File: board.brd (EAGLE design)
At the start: 94.6 x 90.5 mm, 65 parts, among them K1 FTR-K1C, K2 FTR-K1C, K3 FTR-K1C, K4 FTR-K1C, X6 PN61729-S

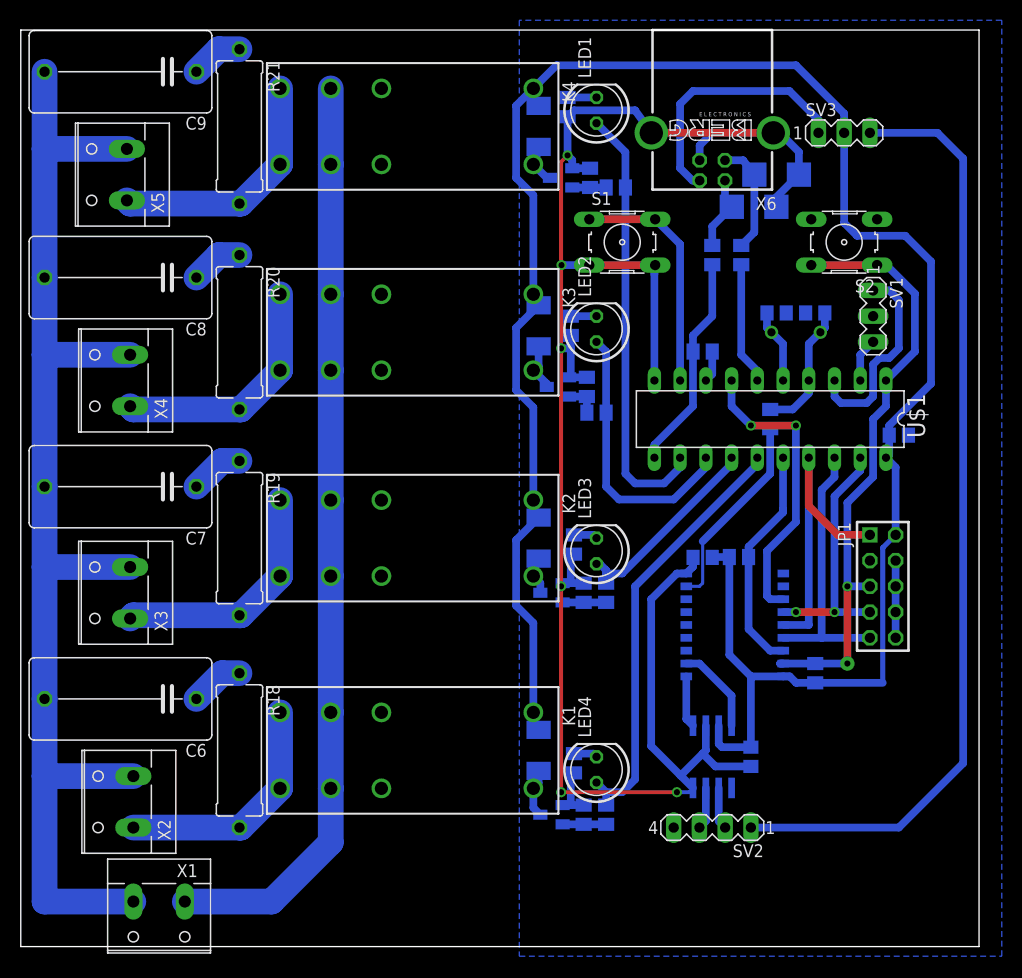
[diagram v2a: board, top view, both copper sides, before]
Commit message: Adding crappy support for a step-down voltage regulator
Well, there should be a different package for the LM2574…
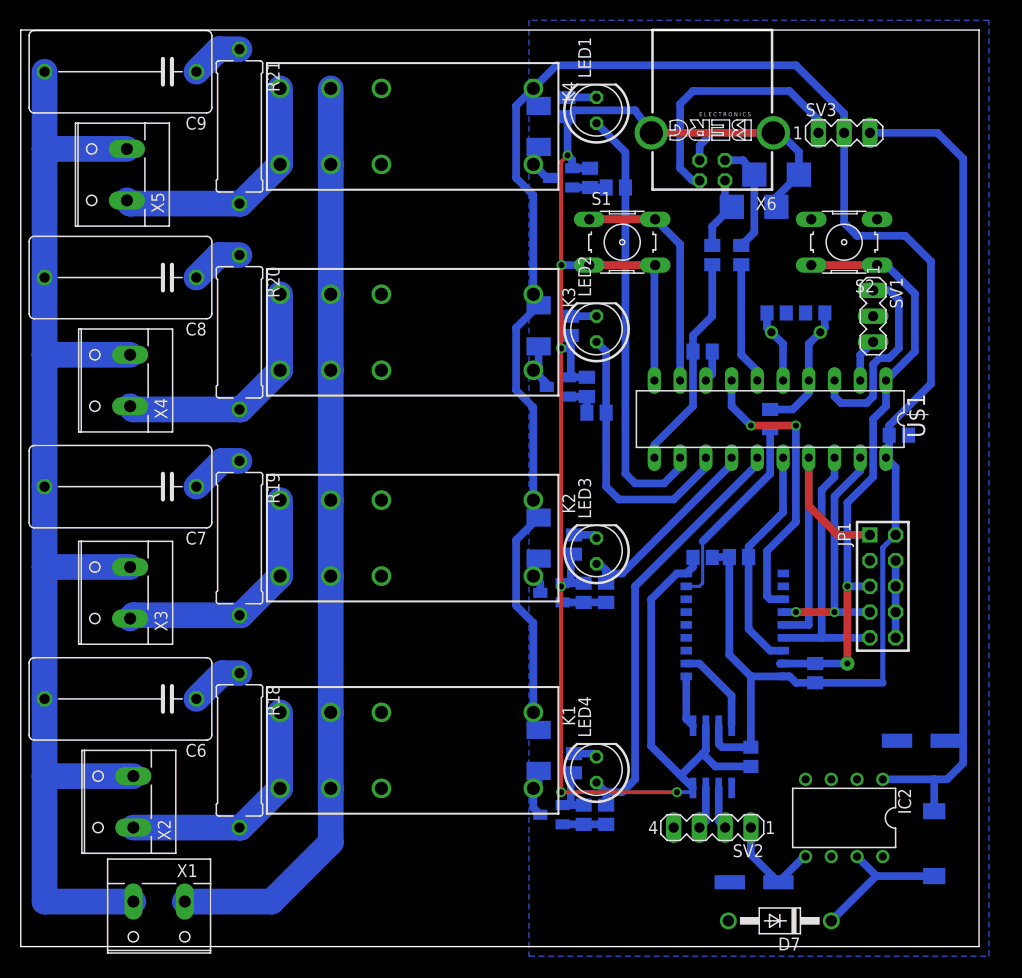
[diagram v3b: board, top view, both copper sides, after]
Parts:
- added C10, C11: (no value), rcl:PANASONIC_D
- added D7: SB120, diode:DO41-10
- added IC2: LM2574HVN-5.0, linear:DIL08
- added L1: (no value), rcl:PIS2816
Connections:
- new net N$38: C10.+, IC2.5, SV2.1
- new net N$8: D7.C, IC2.7, L1.1
- net +5V/2: now also C11.+, IC2.1, L1.2; no longer SV2.1
- net GND: now also C10.-, C11.-, D7.A, IC2.2, IC2.3, IC2.4
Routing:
- net N$8: track 0.00 -> 14.7 mm
- net N$38: track 0.00 -> 10.3 mm
- net +5V/2: track 93.5 -> 83.4 mm
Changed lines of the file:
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@@
 <attribute name="OC_FARNELL" value="unknown" x="68.2625" y="11.7475" size="1.778" layer="27" rot="R180" display="off"/>
 </element>
+<element name="IC2" library="linear" package="DIL08" value="LM2574HVN-5.0" x="81.28" y="12.7" rot="R180"/>
+<element name="C10" library="rcl" package="PANASONIC_D" value="" x="72.39" y="6.35" rot="MR180"/>
+<element name="C11" library="rcl" package="PANASONIC_D" value="" x="88.9" y="20.32" rot="MR180"/>
+<element name="D7" library="diode" package="DO41-10" value="SB120" x="74.93" y="2.54" rot="R180"/>
+<element name="L1" library="rcl" package="PIS2816" value="" x="90.17" y="10.16" rot="MR180"/>
 </elements>
 <signals>
@@
 <via x="53.34" y="35.56" extent="1-16" drill="0.6" shape="square"/>
 <polygon width="0.762" layer="16">
-<vertex x="49.2125" y="91.44"/>
-<vertex x="49.2125" y="-0.9525"/>
-<vertex x="96.8375" y="-0.9525"/>
-<vertex x="96.8375" y="91.44"/>
+<vertex x="50.165" y="91.44"/>
+<vertex x="50.165" y="-0.9525"/>
+<vertex x="95.5675" y="-0.9525"/>
+<vertex x="95.5675" y="91.44"/>
 </polygon>
 <contactref element="C5" pad="1"/>
@@
 <wire x1="54.44" y1="77.64" x2="53.975" y2="78.105" width="0.762" layer="16"/>
 <contactref element="SV2" pad="4"/>
+<contactref element="IC2" pad="4"/>
+<contactref element="IC2" pad="3"/>
+<contactref element="IC2" pad="4"/>
+<contactref element="IC2" pad="2"/>
+<contactref element="C10" pad="-"/>
+<contactref element="C11" pad="-"/>
+<contactref element="D7" pad="A"/>
 <wire x1="86.36" y1="38.1" x2="83.82" y2="38.1" width="0" layer="19" extent="1-1"/>
 <wire x1="53.4875" y1="35.875" x2="53.34" y2="35.56" width="0" layer="19" extent="1-16"/>
@@
 <signal name="+5V/2">
 <contactref element="SV3" pad="3"/>
-<contactref element="SV2" pad="1"/>
 <wire x1="83.82" y1="80.3275" x2="90.4875" y2="80.3275" width="0.762" layer="16"/>
 <wire x1="90.4875" y1="80.3275" x2="93.0275" y2="77.7875" width="0.762" layer="16"/>
-<wire x1="93.0275" y1="77.7875" x2="93.0275" y2="18.0975" width="0.762" layer="16"/>
-<wire x1="93.0275" y1="18.0975" x2="86.6775" y2="11.7475" width="0.762" layer="16"/>
-<wire x1="86.6775" y1="11.7475" x2="72.0725" y2="11.7475" width="0.762" layer="16"/>
+<wire x1="93.0275" y1="77.7875" x2="93.0275" y2="20.32" width="0.762" layer="16"/>
+<contactref element="L1" pad="2"/>
+<contactref element="C11" pad="+"/>
+<contactref element="IC2" pad="1"/>
+<wire x1="93.0275" y1="20.32" x2="93.0275" y2="18.0975" width="0.762" layer="16"/>
+<wire x1="85.09" y1="16.51" x2="90.17" y2="16.51" width="0.762" layer="16"/>
+<wire x1="90.17" y1="16.51" x2="91.44" y2="16.51" width="0.762" layer="16"/>
+<wire x1="91.44" y1="16.51" x2="93.0275" y2="18.0975" width="0.762" layer="16"/>
+<wire x1="91.3" y1="20.32" x2="93.0275" y2="20.32" width="0.762" layer="16"/>
+<wire x1="90.17" y1="13.36" x2="90.17" y2="16.51" width="0.762" layer="16"/>
+</signal>
+<signal name="N$8">
+<contactref element="IC2" pad="7"/>
+<contactref element="L1" pad="1"/>
+<contactref element="D7" pad="C"/>
+<wire x1="82.55" y1="8.89" x2="84.48" y2="6.96" width="0.762" layer="16"/>
+<wire x1="84.48" y1="6.96" x2="90.17" y2="6.96" width="0.762" layer="16"/>
+<wire x1="80.01" y1="2.54" x2="84.43" y2="6.96" width="0.762" layer="16"/>
+<wire x1="84.43" y1="6.96" x2="84.48" y2="6.96" width="0.762" layer="16"/>
+</signal>
+<signal name="N$38">
+<contactref element="SV2" pad="1"/>
+<contactref element="C10" pad="+"/>
+<contactref element="IC2" pad="5"/>
+<wire x1="74.79" y1="6.35" x2="77.33" y2="8.89" width="0.762" layer="16"/>
+<wire x1="77.33" y1="8.89" x2="77.47" y2="8.89" width="0.762" layer="16"/>
+<wire x1="74.79" y1="6.35" x2="72.0725" y2="9.0675" width="0.762" layer="16"/>
+<wire x1="72.0725" y1="9.0675" x2="72.0725" y2="11.7475" width="0.762" layer="16"/>
 </signal>
 </signals>
